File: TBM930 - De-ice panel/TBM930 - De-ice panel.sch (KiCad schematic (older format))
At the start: 69 parts, among them J1 SW_AIRFRAME_DE_ICE, J10 AVR-ISP-6, J11 Screw_Terminal_01x02, J2 SW_ICE_LIGHT, J3 SW_PROP_DE_ICE, J4 SW_WIND_SHIELD, J5 SW_PITOT_L_HTR, J6 SW_PITOT_R_HTR, J7 SW_INERT_SEP, J8 Barrel_Jack, J9 USB_B_Micro, SW1 SW_Push, SW2 SW_Push, U1 TLC5917IN, U2 TLC5917IN, U3 ATmega32U4-MU, Y1 Crystal_GND24

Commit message: Switch to TQFP
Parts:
- U3: footprint Package_DFN_QFN:QFN-44-1EP_7x7mm_P0.5mm_EP5.2x5.2mm -> Package_QFP:TQFP-44-1EP_10x10mm_P0.8mm_EP4.5x4.5mm
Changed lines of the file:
@@
 F 0 "U3" H 2300 1100 50  0000 C CNN
 F 1 "ATmega32U4-MU" H 2350 1200 50  0000 C CNN
-F 2 "Package_DFN_QFN:QFN-44-1EP_7x7mm_P0.5mm_EP5.2x5.2mm" H 1950 700 50  0001 C CIN
+F 2 "Package_QFP:TQFP-44-1EP_10x10mm_P0.8mm_EP4.5x4.5mm" H 1950 700 50  0001 C CIN
 F 3 "http://ww1.microchip.com/downloads/en/DeviceDoc/Atmel-7766-8-bit-AVR-ATmega16U4-32U4_Datasheet.pdf" H 1950 2950 50  0001 C CNN
 F 4 "VQFN-44_EP_7.0x7.0x0.5P" H 1950 2950 50  0001 C CNN "JLC"

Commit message: Lots of minor updates to silk screen and vias
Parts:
- D1, D2, D3: footprint LED_SMD:LED_0603_1608Metric -> Global MobiFlight panel parts:LED_0603_1608Metric
- D10, D11, D12, D13, D14, D15, D16, D18, D19, D20, D21, D22, D23, D24, D25, D26, D27, D9: footprint LED_SMD:LED_1206_3216Metric_Pad1.42x1.75mm_HandSolder -> Global MobiFlight panel parts:LED_1206_3216Metric_Pad1.42x1.75mm_HandSolder
- SW1, SW2: JLC 0603 -> (none)
- U3: JLC VQFN-44_EP_7.0x7.0x0.5P -> (none); LCSC C112161 -> (none)
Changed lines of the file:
@@
 F 0 "D9" H 6443 2195 50  0000 C CNN
 F 1 "LED" H 6443 2286 50  0000 C CNN
-F 2 "LED_SMD:LED_1206_3216Metric_Pad1.42x1.75mm_HandSolder" H 6450 2450 50  0001 C CNN
+F 2 "Global MobiFlight panel parts:LED_1206_3216Metric_Pad1.42x1.75mm_HandSolder" H 6450 2450 50  0001 C CNN
 F 3 "~" H 6450 2450 50  0001 C CNN
 F 4 "" H 6450 2450 50  0001 C CNN "JLC"
@@
 F 0 "D10" H 6743 2195 50  0000 C CNN
 F 1 "LED" H 6743 2286 50  0000 C CNN
-F 2 "LED_SMD:LED_1206_3216Metric_Pad1.42x1.75mm_HandSolder" H 6750 2450 50  0001 C CNN
+F 2 "Global MobiFlight panel parts:LED_1206_3216Metric_Pad1.42x1.75mm_HandSolder" H 6750 2450 50  0001 C CNN
 F 3 "~" H 6750 2450 50  0001 C CNN
 F 4 "" H 6750 2450 50  0001 C CNN "JLC"
@@
 F 0 "D11" H 7043 2195 50  0000 C CNN
 F 1 "LED" H 7043 2286 50  0000 C CNN
-F 2 "LED_SMD:LED_1206_3216Metric_Pad1.42x1.75mm_HandSolder" H 7050 2450 50  0001 C CNN
+F 2 "Global MobiFlight panel parts:LED_1206_3216Metric_Pad1.42x1.75mm_HandSolder" H 7050 2450 50  0001 C CNN
 F 3 "~" H 7050 2450 50  0001 C CNN
 F 4 "" H 7050 2450 50  0001 C CNN "JLC"
@@
 F 0 "D13" H 6743 2645 50  0000 C CNN
 F 1 "LED" H 6743 2736 50  0000 C CNN
-F 2 "LED_SMD:LED_1206_3216Metric_Pad1.42x1.75mm_HandSolder" H 6750 2900 50  0001 C CNN
+F 2 "Global MobiFlight panel parts:LED_1206_3216Metric_Pad1.42x1.75mm_HandSolder" H 6750 2900 50  0001 C CNN
 F 3 "~" H 6750 2900 50  0001 C CNN
 F 4 "" H 6750 2900 50  0001 C CNN "JLC"
@@
 F 0 "D14" H 7043 2645 50  0000 C CNN
 F 1 "LED" H 7043 2736 50  0000 C CNN
-F 2 "LED_SMD:LED_1206_3216Metric_Pad1.42x1.75mm_HandSolder" H 7050 2900 50  0001 C CNN
+F 2 "Global MobiFlight panel parts:LED_1206_3216Metric_Pad1.42x1.75mm_HandSolder" H 7050 2900 50  0001 C CNN
 F 3 "~" H 7050 2900 50  0001 C CNN
 F 4 "" H 7050 2900 50  0001 C CNN "JLC"
@@
 F 0 "D15" H 6443 3145 50  0000 C CNN
 F 1 "LED" H 6443 3236 50  0000 C CNN
-F 2 "LED_SMD:LED_1206_3216Metric_Pad1.42x1.75mm_HandSolder" H 6450 3400 50  0001 C CNN
+F 2 "Global MobiFlight panel parts:LED_1206_3216Metric_Pad1.42x1.75mm_HandSolder" H 6450 3400 50  0001 C CNN
 F 3 "~" H 6450 3400 50  0001 C CNN
 F 4 "" H 6450 3400 50  0001 C CNN "JLC"
@@
 F 0 "D16" H 6743 3145 50  0000 C CNN
 F 1 "LED" H 6743 3236 50  0000 C CNN
-F 2 "LED_SMD:LED_1206_3216Metric_Pad1.42x1.75mm_HandSolder" H 6750 3400 50  0001 C CNN
+F 2 "Global MobiFlight panel parts:LED_1206_3216Metric_Pad1.42x1.75mm_HandSolder" H 6750 3400 50  0001 C CNN
 F 3 "~" H 6750 3400 50  0001 C CNN
 F 4 "" H 6750 3400 50  0001 C CNN "JLC"
@@
 F 0 "D18" H 6443 3645 50  0000 C CNN
 F 1 "LED" H 6443 3736 50  0000 C CNN
-F 2 "LED_SMD:LED_1206_3216Metric_Pad1.42x1.75mm_HandSolder" H 6450 3900 50  0001 C CNN
+F 2 "Global MobiFlight panel parts:LED_1206_3216Metric_Pad1.42x1.75mm_HandSolder" H 6450 3900 50  0001 C CNN
 F 3 "~" H 6450 3900 50  0001 C CNN
 F 4 "" H 6450 3900 50  0001 C CNN "JLC"
@@
 F 0 "D19" H 6743 3645 50  0000 C CNN
 F 1 "LED" H 6743 3736 50  0000 C CNN
-F 2 "LED_SMD:LED_1206_3216Metric_Pad1.42x1.75mm_HandSolder" H 6750 3900 50  0001 C CNN
+F 2 "Global MobiFlight panel parts:LED_1206_3216Metric_Pad1.42x1.75mm_HandSolder" H 6750 3900 50  0001 C CNN
 F 3 "~" H 6750 3900 50  0001 C CNN
 F 4 "" H 6750 3900 50  0001 C CNN "JLC"
@@
 F 0 "D20" H 7043 3645 50  0000 C CNN
 F 1 "LED" H 7043 3736 50  0000 C CNN
-F 2 "LED_SMD:LED_1206_3216Metric_Pad1.42x1.75mm_HandSolder" H 7050 3900 50  0001 C CNN
+F 2 "Global MobiFlight panel parts:LED_1206_3216Metric_Pad1.42x1.75mm_HandSolder" H 7050 3900 50  0001 C CNN
 F 3 "~" H 7050 3900 50  0001 C CNN
 F 4 "" H 7050 3900 50  0001 C CNN "JLC"
@@
 F 0 "D21" H 6443 4145 50  0000 C CNN
 F 1 "LED" H 6443 4236 50  0000 C CNN
-F 2 "LED_SMD:LED_1206_3216Metric_Pad1.42x1.75mm_HandSolder" H 6450 4400 50  0001 C CNN
+F 2 "Global MobiFlight panel parts:LED_1206_3216Metric_Pad1.42x1.75mm_HandSolder" H 6450 4400 50  0001 C CNN
 F 3 "~" H 6450 4400 50  0001 C CNN
 F 4 "" H 6450 4400 50  0001 C CNN "JLC"
@@
 F 0 "D22" H 6743 4145 50  0000 C CNN
 F 1 "LED" H 6743 4236 50  0000 C CNN
-F 2 "LED_SMD:LED_1206_3216Metric_Pad1.42x1.75mm_HandSolder" H 6750 4400 50  0001 C CNN
+F 2 "Global MobiFlight panel parts:LED_1206_3216Metric_Pad1.42x1.75mm_HandSolder" H 6750 4400 50  0001 C CNN
 F 3 "~" H 6750 4400 50  0001 C CNN
 F 4 "" H 6750 4400 50  0001 C CNN "JLC"
@@
 F 0 "D23" H 7043 4145 50  0000 C CNN
 F 1 "LED" H 7043 4236 50  0000 C CNN
-F 2 "LED_SMD:LED_1206_3216Metric_Pad1.42x1.75mm_HandSolder" H 7050 4400 50  0001 C CNN
+F 2 "Global MobiFlight panel parts:LED_1206_3216Metric_Pad1.42x1.75mm_HandSolder" H 7050 4400 50  0001 C CNN
 F 3 "~" H 7050 4400 50  0001 C CNN
 F 4 "" H 7050 4400 50  0001 C CNN "JLC"
@@
 F 0 "D24" H 6443 4595 50  0000 C CNN
 F 1 "LED" H 6443 4686 50  0000 C CNN
-F 2 "LED_SMD:LED_1206_3216Metric_Pad1.42x1.75mm_HandSolder" H 6450 4850 50  0001 C CNN
+F 2 "Global MobiFlight panel parts:LED_1206_3216Metric_Pad1.42x1.75mm_HandSolder" H 6450 4850 50  0001 C CNN
 F 3 "~" H 6450 4850 50  0001 C CNN
 F 4 "" H 6450 4850 50  0001 C CNN "JLC"
@@
 F 0 "D25" H 6743 4595 50  0000 C CNN
 F 1 "LED" H 6743 4686 50  0000 C CNN
-F 2 "LED_SMD:LED_1206_3216Metric_Pad1.42x1.75mm_HandSolder" H 6750 4850 50  0001 C CNN
+F 2 "Global MobiFlight panel parts:LED_1206_3216Metric_Pad1.42x1.75mm_HandSolder" H 6750 4850 50  0001 C CNN
 F 3 "~" H 6750 4850 50  0001 C CNN
 F 4 "" H 6750 4850 50  0001 C CNN "JLC"
@@
 F 0 "D26" H 6443 5095 50  0000 C CNN
 F 1 "LED" H 6443 5186 50  0000 C CNN
-F 2 "LED_SMD:LED_1206_3216Metric_Pad1.42x1.75mm_HandSolder" H 6450 5350 50  0001 C CNN
+F 2 "Global MobiFlight panel parts:LED_1206_3216Metric_Pad1.42x1.75mm_HandSolder" H 6450 5350 50  0001 C CNN
 F 3 "~" H 6450 5350 50  0001 C CNN
 F 4 "" H 6450 5350 50  0001 C CNN "JLC"
@@
 F 0 "D27" H 6743 5095 50  0000 C CNN
 F 1 "LED" H 6743 5186 50  0000 C CNN
-F 2 "LED_SMD:LED_1206_3216Metric_Pad1.42x1.75mm_HandSolder" H 6750 5350 50  0001 C CNN
+F 2 "Global MobiFlight panel parts:LED_1206_3216Metric_Pad1.42x1.75mm_HandSolder" H 6750 5350 50  0001 C CNN
 F 3 "~" H 6750 5350 50  0001 C CNN
 F 4 "" H 6750 5350 50  0001 C CNN "JLC"
@@
 F 0 "D3" V 2589 5882 50  0000 R CNN
 F 1 "GREEN" V 2498 5882 50  0000 R CNN
-F 2 "LED_SMD:LED_0603_1608Metric" H 2550 6000 50  0001 C CNN
+F 2 "Global MobiFlight panel parts:LED_0603_1608Metric" H 2550 6000 50  0001 C CNN
 F 3 "~" H 2550 6000 50  0001 C CNN
 F 4 "LED_0603" H 2550 6000 50  0001 C CNN "JLC"
@@
 F 0 "D2" V 3639 3482 50  0000 R CNN
 F 1 "GREEN" V 3548 3482 50  0000 R CNN
-F 2 "LED_SMD:LED_0603_1608Metric" H 3600 3600 50  0001 C CNN
+F 2 "Global MobiFlight panel parts:LED_0603_1608Metric" H 3600 3600 50  0001 C CNN
 F 3 "~" H 3600 3600 50  0001 C CNN
 F 4 "LED_0603" H 3600 3600 50  0001 C CNN "JLC"
@@
 F 0 "D1" V 3639 1782 50  0000 R CNN
 F 1 "YELLOW" V 3548 1782 50  0000 R CNN
-F 2 "LED_SMD:LED_0603_1608Metric" H 3600 1900 50  0001 C CNN
+F 2 "Global MobiFlight panel parts:LED_0603_1608Metric" H 3600 1900 50  0001 C CNN
 F 3 "~" H 3600 1900 50  0001 C CNN
 F 4 "LED_0603" H 3600 1900 50  0001 C CNN "JLC"
@@
 F 0 "D12" H 6443 2645 50  0000 C CNN
 F 1 "LED" H 6443 2736 50  0000 C CNN
-F 2 "LED_SMD:LED_1206_3216Metric_Pad1.42x1.75mm_HandSolder" H 6450 2900 50  0001 C CNN
+F 2 "Global MobiFlight panel parts:LED_1206_3216Metric_Pad1.42x1.75mm_HandSolder" H 6450 2900 50  0001 C CNN
 F 3 "~" H 6450 2900 50  0001 C CNN
 F 4 "" H 6450 2900 50  0001 C CNN "JLC"
@@
 F 2 "Package_QFP:TQFP-44-1EP_10x10mm_P0.8mm_EP4.5x4.5mm" H 1950 700 50  0001 C CIN
 F 3 "http://ww1.microchip.com/downloads/en/DeviceDoc/Atmel-7766-8-bit-AVR-ATmega16U4-32U4_Datasheet.pdf" H 1950 2950 50  0001 C CNN
-F 4 "VQFN-44_EP_7.0x7.0x0.5P" H 1950 2950 50  0001 C CNN "JLC"
-F 5 "C112161" H 1950 2950 50  0001 C CNN "LCSC"
+F 4 "" H 1950 2950 50  0001 C CNN "JLC"
+F 5 "" H 1950 2950 50  0001 C CNN "LCSC"
 	1    1950 2950
 	1    0    0    -1
@@
 F 2 "Button_Switch_THT:SW_PUSH_6mm_H4.3mm" H 5400 7500 50  0001 C CNN
 F 3 "~" H 5400 7500 50  0001 C CNN
-F 4 "0603" H 5400 7300 50  0001 C CNN "JLC"
+F 4 "" H 5400 7300 50  0001 C CNN "JLC"
 	1    5400 7300
 	1    0    0    -1
@@
 F 2 "Button_Switch_THT:SW_PUSH_6mm_H9.5mm" H 9200 4000 50  0001 C CNN
 F 3 "~" H 9200 4000 50  0001 C CNN
-F 4 "0603" H 9200 3800 50  0001 C CNN "JLC"
+F 4 "" H 9200 3800 50  0001 C CNN "JLC"
 	1    9200 3800
 	1    0    0    -1

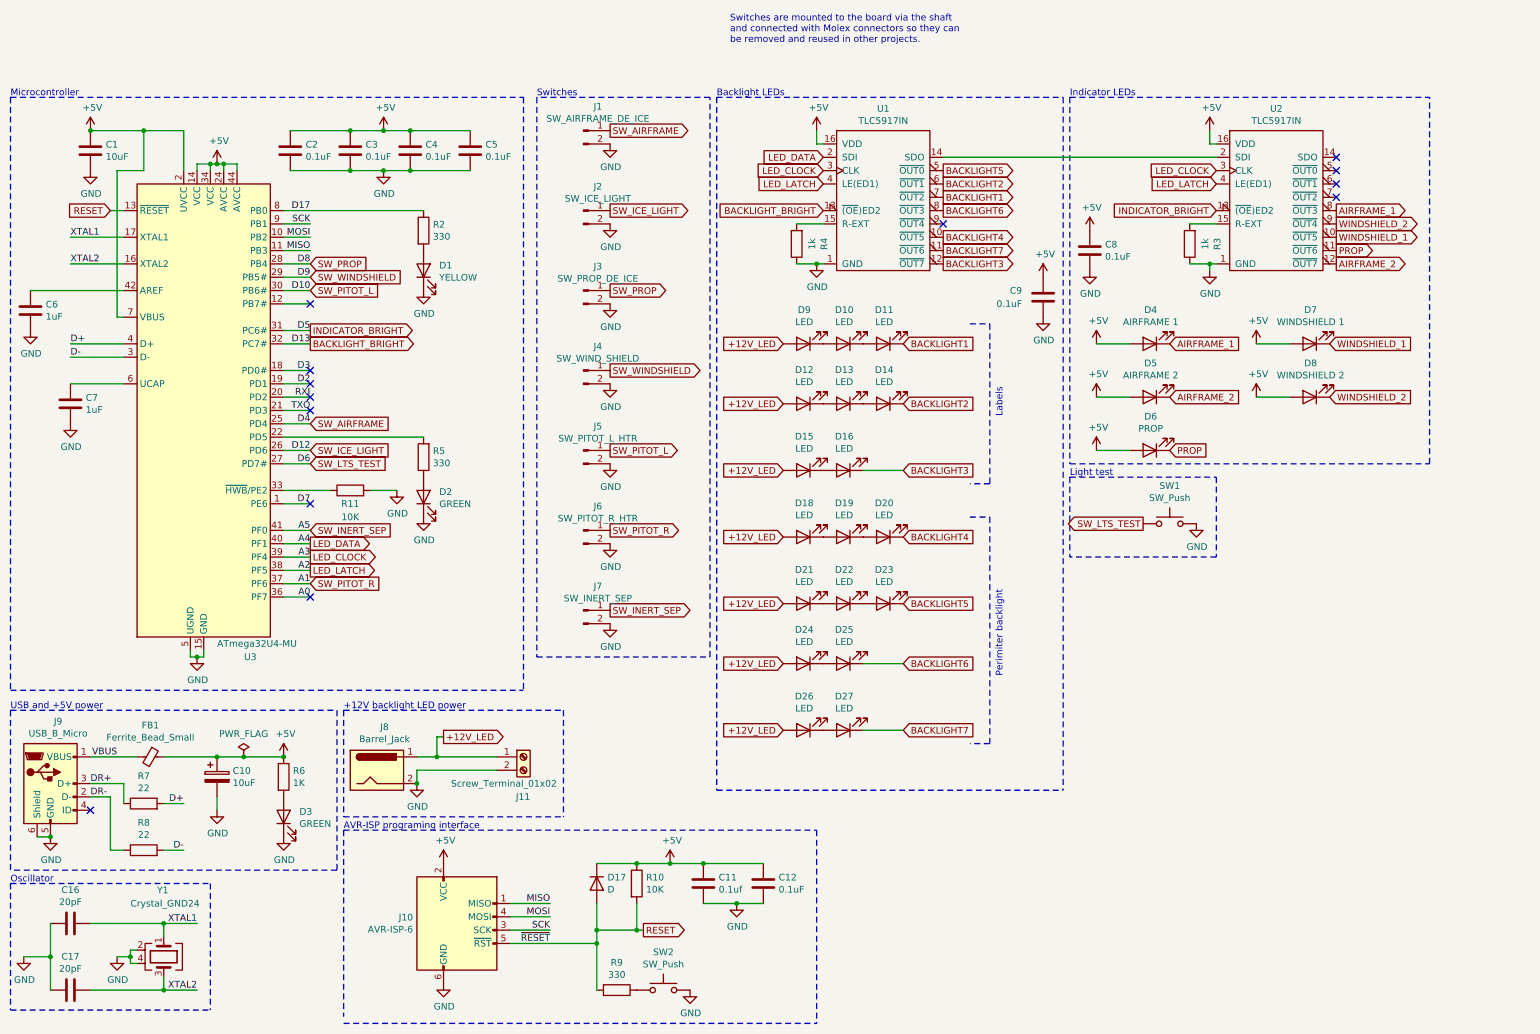
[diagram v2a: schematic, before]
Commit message: Adjust the spacing of PCB components, reroute data trace
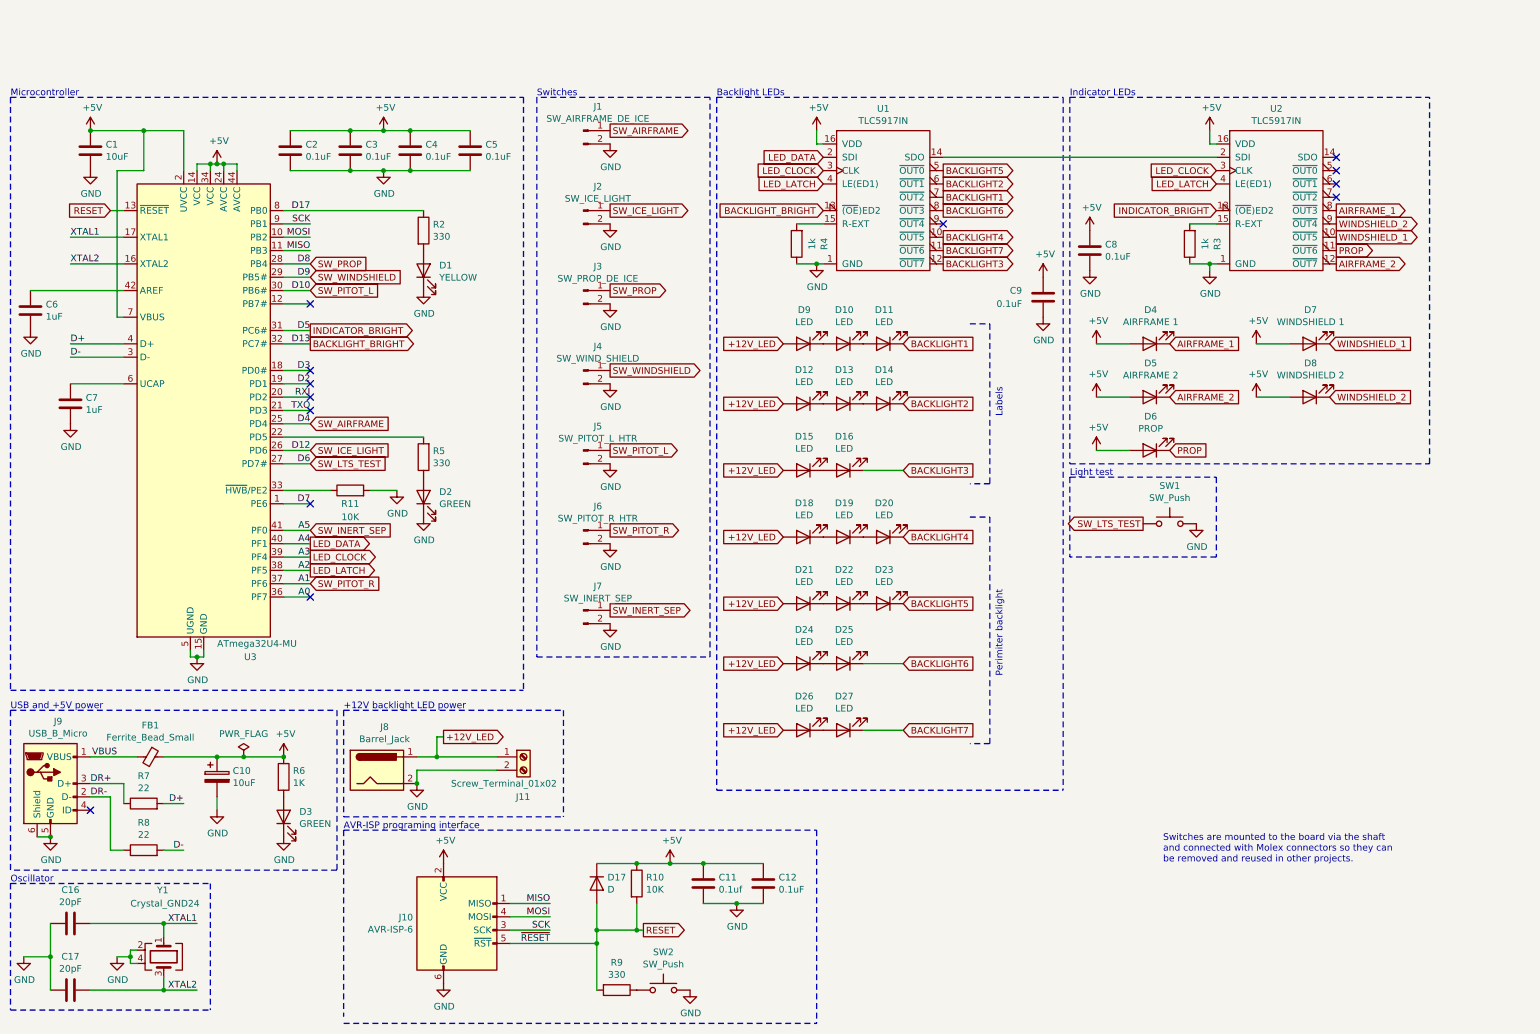
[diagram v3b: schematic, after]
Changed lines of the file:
@@
 	1    0    0    -1
 $EndComp
-Text Notes 5900 200  0    50   ~ 0
+Text Notes 9150 6350 0    50   ~ 0
 Switches are mounted to the board via the shaft\nand connected with Molex connectors so they can\nbe removed and reused in other projects.\n
 $Comp
